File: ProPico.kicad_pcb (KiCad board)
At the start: 2 copper layers, 21 x 51 mm, 56 parts, among them J1 USB_C_Receptacle_USB2.0, J2 SWD, J3 LEFT, J4 RIGHT, SW1 BOOTSEL, SW2 RES, U1 FM24CL16B, U2 W25Q16JVUXIQ, U3 AMS1117-3.3, U4 LM4040DBZ-3, U5 RP2040, Y1 ECS-120-12-36-AGN-TR3

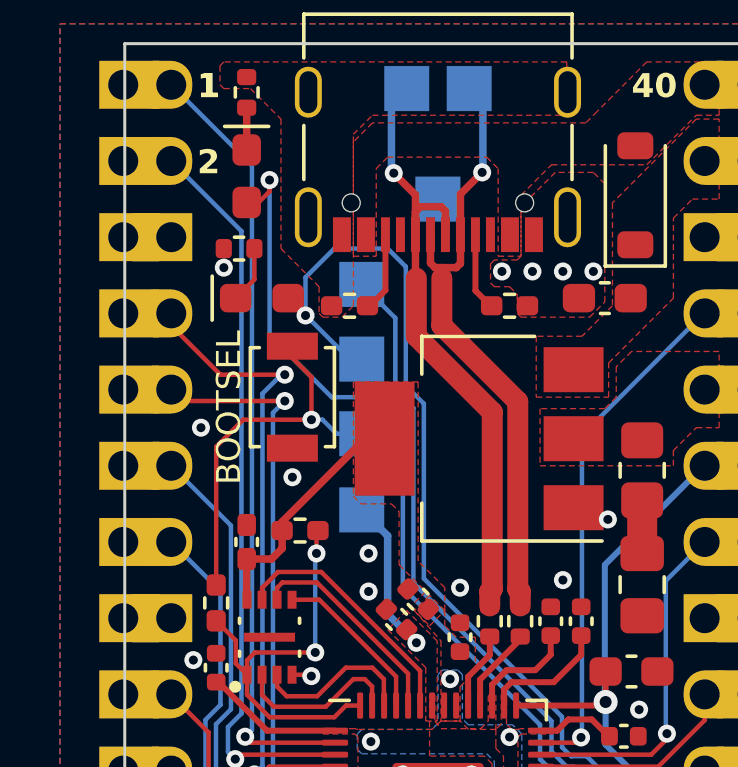
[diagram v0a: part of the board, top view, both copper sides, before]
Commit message: added critical feature; neopixel
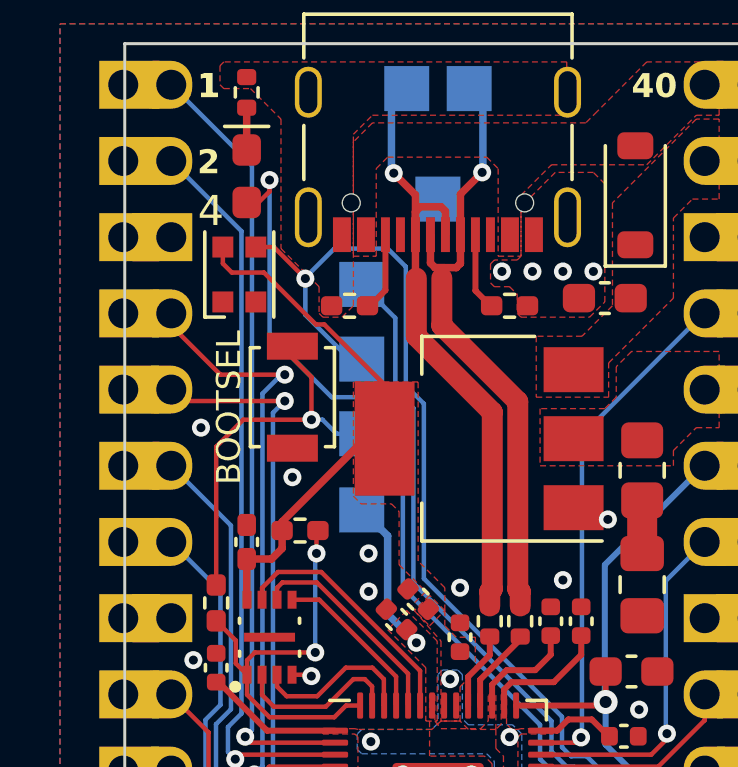
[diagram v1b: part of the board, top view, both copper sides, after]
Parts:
- removed D3: LED, LED_SMD:LED_0603_1608Metric_Pad1.05x0.95mm_HandSolder
- removed R13: 1k, Resistor_SMD:R_0402_1005Metric
- added 4: WS2812B-2020, LED_SMD:LED_WS2812B-2020_PLCC4_2.0x2.0mm, F.Cu at (96.2, 47.0)
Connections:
- J4 pad 15: /ADC_VREF -> (no net)
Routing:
- net +3V3: track 65.0 -> 74.5 mm
- net Net-(D3-K): track 1.91 -> 0.00 mm
- net /EEPROM_SCL: track 51.8 -> 53.0 mm
- net GND: vias 30 -> 29
